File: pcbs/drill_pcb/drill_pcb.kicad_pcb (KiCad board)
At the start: 2 copper layers, 240 x 100 mm, 70 parts, among them SW101 RPi reset, U1 FXMA108, U102 Pico, U201 IFX007T, U202 IFX007T, U203 ACS712xLCTR-20A, U401 HT75xx-1-SOT89

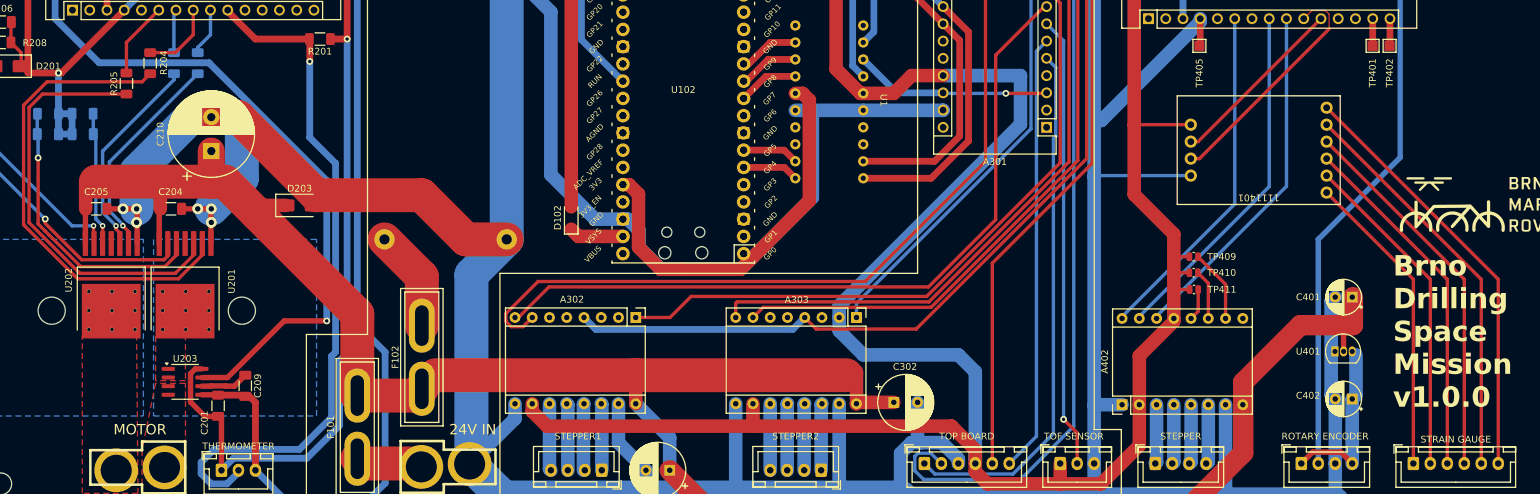
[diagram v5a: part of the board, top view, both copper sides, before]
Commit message: PCB update Fixed connector silkscreen. Added H-bridge capacitors.
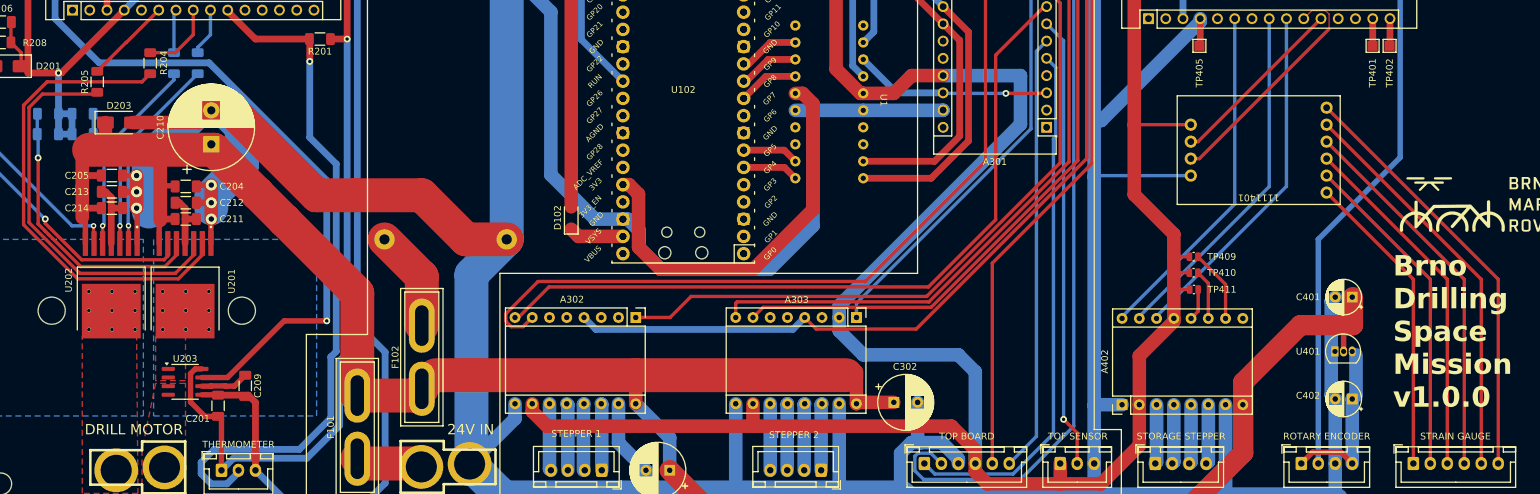
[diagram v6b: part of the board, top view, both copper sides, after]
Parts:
- added C211: 100n/50V, Capacitor_SMD:C_1206_3216Metric_Pad1.33x1.80mm_HandSolder, F.Cu at (127.2, 151.0)
- added C212: 100n/50V, Capacitor_SMD:C_1206_3216Metric_Pad1.33x1.80mm_HandSolder, F.Cu at (127.2, 148.6)
- added C213: 100n/50V, Capacitor_SMD:C_1206_3216Metric_Pad1.33x1.80mm_HandSolder, F.Cu at (116.4, 147.0)
- added C214: 100n/50V, Capacitor_SMD:C_1206_3216Metric_Pad1.33x1.80mm_HandSolder, F.Cu at (116.4, 149.4)
- Dean101: renamed from 24V IN
- Dean201: renamed from MOTOR; value Motor -> DRILL MOTOR
- J201: renamed from THERMOMETER; value Thermometer -> THERMOMETER
- J301: renamed from TOP BOARD; value Screw_Terminal_01x06 -> TOP BOARD
- J302: renamed from STEPPER1; value motor1 -> STEPPER 1
- J306: renamed from STEPPER2; value motor2 -> STEPPER 2
- J307: renamed from TOF SENSOR; value TOF_senzor -> TOF SENSOR
- J401: renamed from ROTARY ENCODER; value Screw_Terminal_01x04 -> ROTARY ENCODER
- J402: renamed from STRAIN GAUGE; value Screw_Terminal_01x06 -> STRAIN GAUGE
- J403: renamed from STEPPER; value Screw_Terminal_01x04 -> STORAGE STEPPER
- moved D203 29.3 mm to (117.4, 136.8)
- moved C205 5.41 mm to (116.4, 144.6)
- moved R205 4.31 mm to (114.2, 130.8)
- moved C204 3.95 mm to (127.2, 146.2)
- moved C210 1.00 mm to (131.0, 140.0)
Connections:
- U1 pad 1: GND -> +3.3V
- U102 pad 1: GND -> unconnected-(U102-GPIO0-Pad1)_1
- U102 pad 36: GND -> +3.3V
- U201 pad 4: unconnected-(U201-OUT-Pad4) -> Net-(C211-Pad1)
- U202 pad 4: unconnected-(U202-OUT-Pad4) -> Net-(C213-Pad2)
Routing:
- net +3.3V: track 0.00 -> 60.2 mm
- net GND: track 1031.9 -> 998.0 mm
- net +24V: track 314.4 -> 334.5 mm
- net Net-(C213-Pad2): track 0.00 -> 10.3 mm
- net Net-(C211-Pad1): track 0.00 -> 8.66 mm
- net Net-(U201-INH): track 62.3 -> 58.1 mm
- net Net-(U202-IN): track 31.6 -> 29.3 mm
- net Net-(U202-INH): track 30.4 -> 28.3 mm
- net Net-(A201-D3): track 11.2 -> 12.8 mm

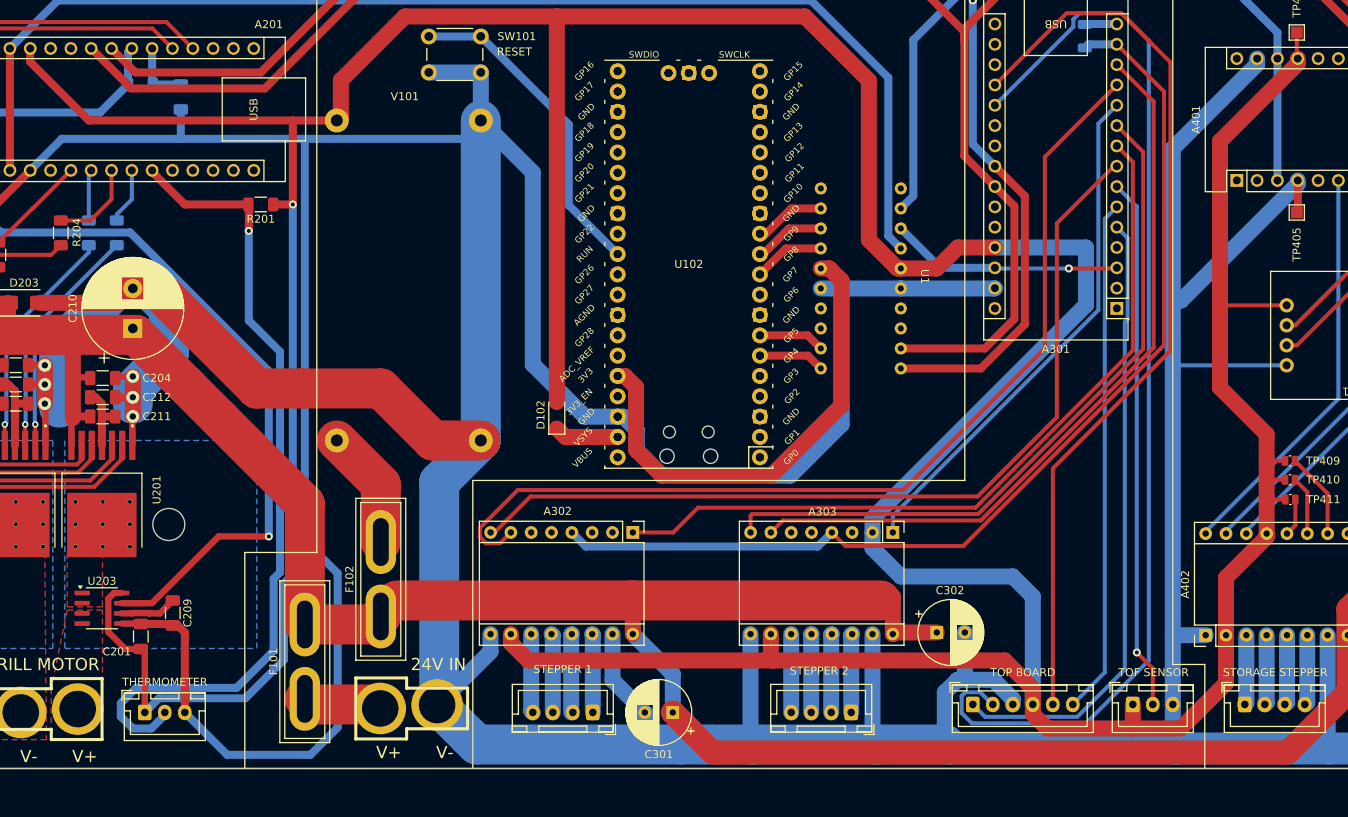
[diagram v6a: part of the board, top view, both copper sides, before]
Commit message: PCB update Stepper drivers moved to make space for RPi USB cable.
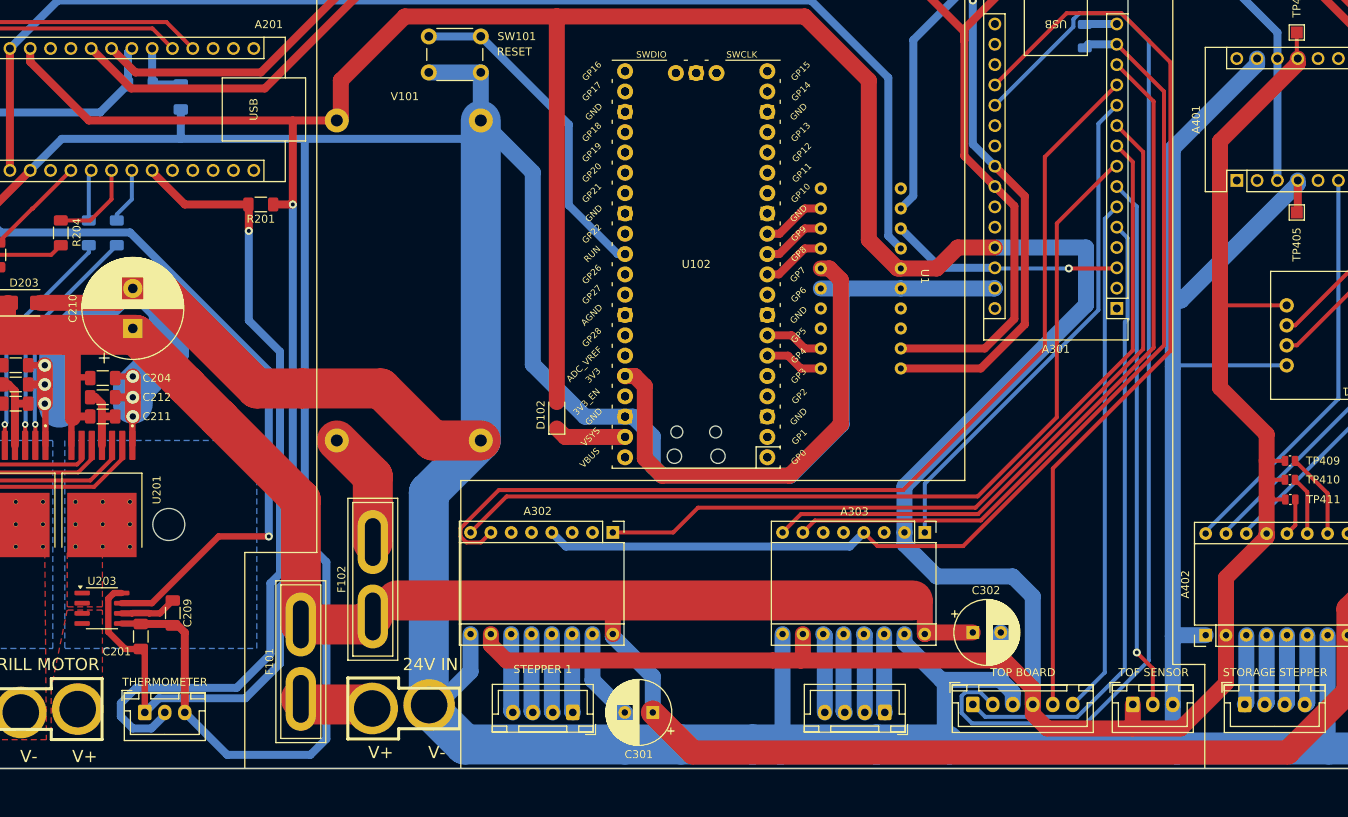
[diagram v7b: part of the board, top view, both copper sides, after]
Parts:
- moved C302 4.50 mm to (236.0, 178.0)
- moved J306 4.20 mm to (225.0, 188.0)
- moved A303 4.00 mm to (230.0, 165.5)
- moved A302 2.50 mm to (191.0, 165.5)
- moved C301 2.50 mm to (196.0, 188.0)
- moved J302 2.50 mm to (186.0, 188.0)
- moved Dean101 1.00 mm to (165.5, 187.5)
- moved F102 1.00 mm to (161.0, 176.0)
- moved U102 0.93 mm to (201.4, 132.0)
- moved F101 0.50 mm to (152.0, 186.3)
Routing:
- net +24V: track 334.5 -> 354.7 mm
- net GND: track 998.0 -> 989.1 mm
- net Net-(A301-D7): track 89.1 -> 83.9 mm
- net Net-(A301-D10): track 94.7 -> 90.7 mm
- net +5V: track 623.7 -> 620.4 mm
- net Net-(A301-D6): track 98.3 -> 100.8 mm
- net Net-(A301-D5): track 111.4 -> 113.9 mm
- net Net-(A301-D11): track 130.8 -> 133.3 mm
- net Net-(A301-D9): track 122.5 -> 124.7 mm
- net Net-(A301-D8): track 65.0 -> 63.3 mm
- net +3.3V: track 60.2 -> 61.3 mm
- net Net-(U1-A3): track 8.95 -> 8.03 mm
- net Net-(U1-A1): track 8.92 -> 7.99 mm
- net Net-(U1-A7): track 8.27 -> 7.35 mm
- net Net-(U1-A2): track 8.94 -> 8.01 mm
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
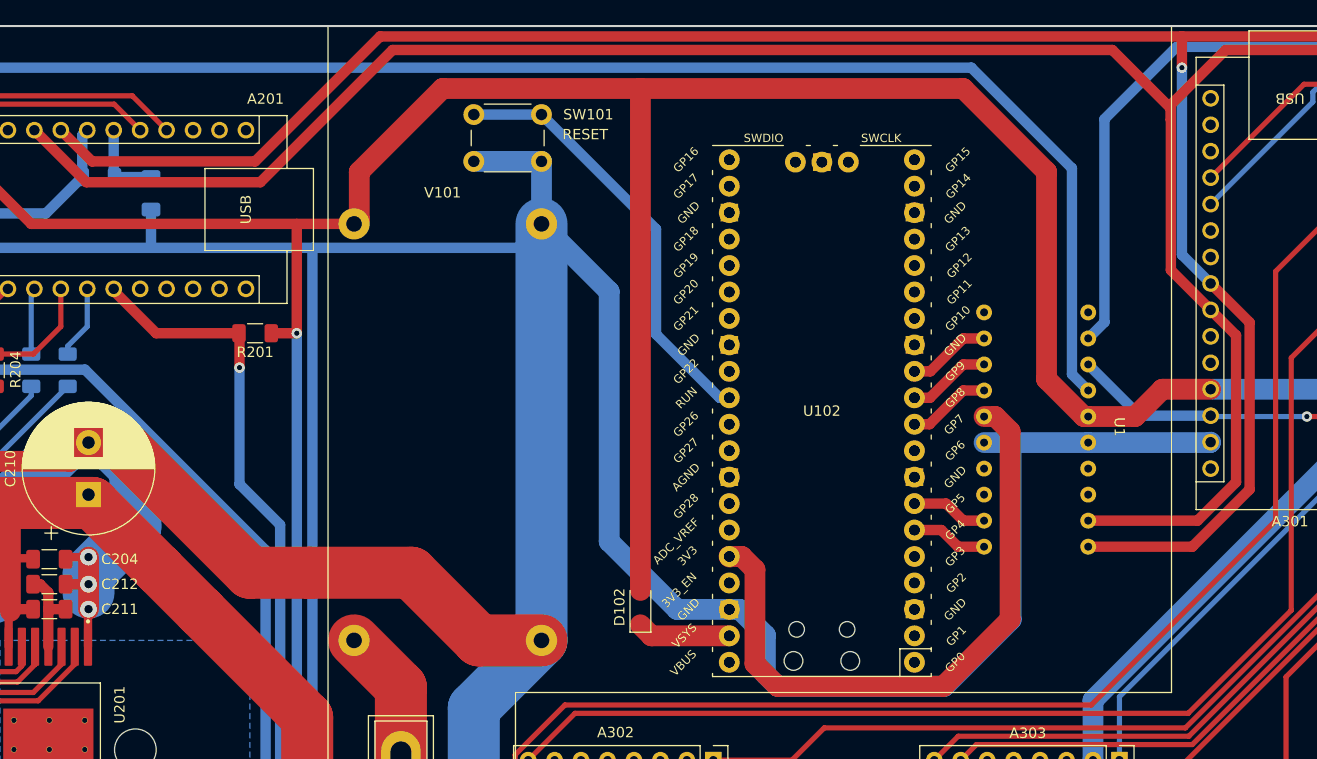
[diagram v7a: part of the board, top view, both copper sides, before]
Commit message: PCB update swapped level shifter board for IC
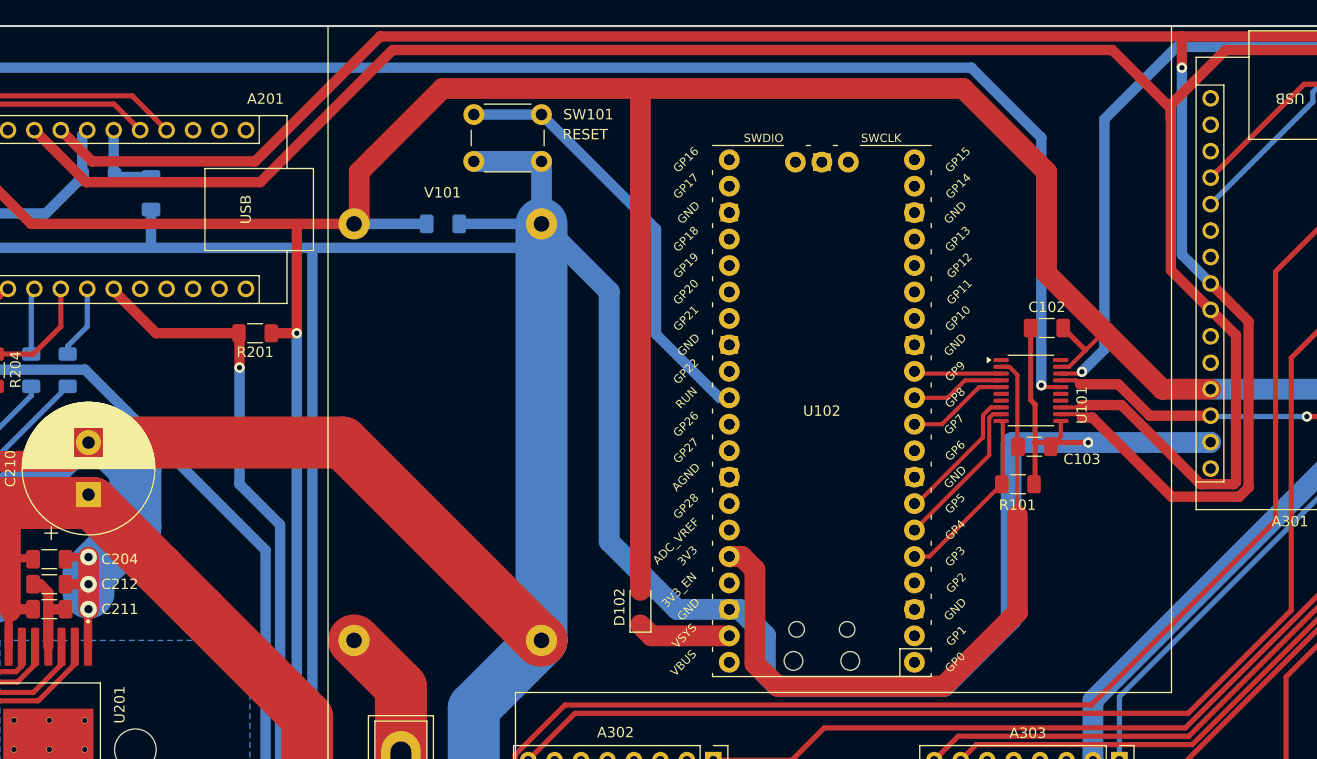
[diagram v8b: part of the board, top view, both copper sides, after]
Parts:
- removed U1: FXMA108, drill_i2c_level_shifter:logic_convertor_8ch
- added C101: 100n, Capacitor_SMD:C_1206_3216Metric_Pad1.33x1.80mm_HandSolder, B.Cu at (165.0, 114.0)
- added C102: 100n, Capacitor_SMD:C_1206_3216Metric_Pad1.33x1.80mm_HandSolder, F.Cu at (223.0, 124.0)
- added C103: 100n, Capacitor_SMD:C_1206_3216Metric_Pad1.33x1.80mm_HandSolder, F.Cu at (221.8, 135.4)
- added R101: 10k, Resistor_SMD:R_1206_3216Metric_Pad1.30x1.75mm_HandSolder, F.Cu at (220.2, 139.0)
- added U101: TXS0108EPW, Package_SO:TSSOP-20_4.4x6.5mm_P0.65mm, F.Cu at (221.5, 130.0)
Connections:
- U102 pad 5: unconnected-(U102-GPIO3-Pad5)_1 -> Net-(U101-OE)
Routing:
- net GND: track 989.1 -> 1018.7 mm, vias 7 -> 8
- net Net-(U101-OE): track 0.00 -> 17.4 mm
- net Net-(U101-A8): track 7.35 -> 15.0 mm
- net +5V: track 620.4 -> 627.9 mm
- net Net-(U101-A7): track 7.36 -> 13.4 mm
- net /Storage and weighing/RESET: track 91.1 -> 96.6 mm, vias 0 -> 1
- net /Linear drive control/SCL: track 231.5 -> 236.0 mm
- net +3.3V: track 61.3 -> 65.7 mm
- net /Linear drive control/SDA: track 234.8 -> 238.5 mm
- net /Linear drive control/RESET: track 29.1 -> 31.1 mm
- net Net-(U101-A4): track 8.03 -> 9.80 mm
- net Net-(U101-A3): track 8.01 -> 9.02 mm
- net /Motor control/RESET: track 153.5 -> 153.1 mm, vias 0 -> 1
